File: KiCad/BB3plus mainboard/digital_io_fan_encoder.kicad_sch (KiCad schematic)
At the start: 51 parts, among them IC10 THVD1420DR, IC11 TPD4E001DRLR, IC12 TPD4E001DRLR, IC7 EMC2301-1-ACZL-TR, IC8 ISO6763FDWR, IC9 BD00FC0W, SW2 PEC16-2215F-S0024, X13 22-27-2031, X14 TBP03R1-350-10BE

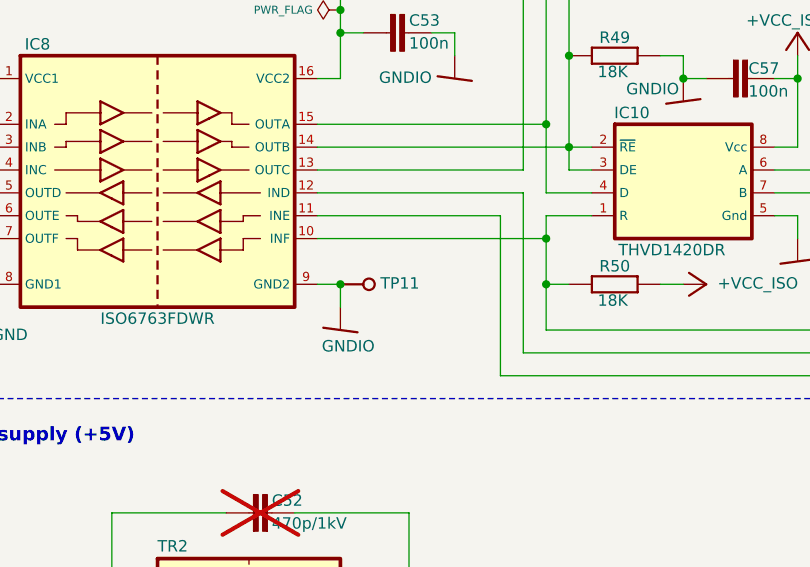
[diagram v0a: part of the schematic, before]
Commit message: Rear USB & Ethernet updated
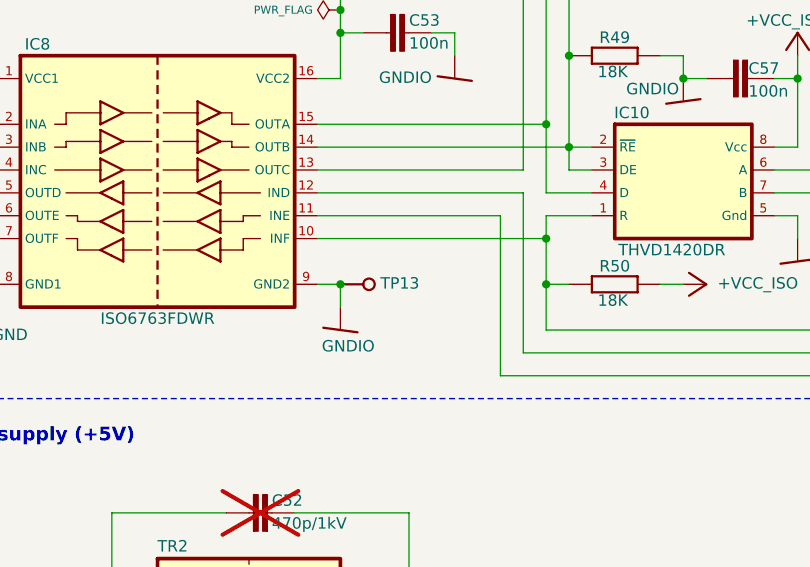
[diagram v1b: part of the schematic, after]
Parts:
- renumbered TP11 to TP13
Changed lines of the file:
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@@
 		(in_bom no)
 		(on_board yes)
-		(in_pos_files yes)
+		(in_pos_files no)
 		(dnp no)
-		(property "Reference" "TP11"
+		(property "Reference" "TP13"
 			(at 90.805 71.755 0)
 			(show_name no)
@@
 			(project "BB3plus mainboard"
 				(path "/1df84e4f-233a-4f72-9418-c0020706bb76/830c9101-e201-40d1-8c34-0dbed89b71c3"
-					(reference "TP11")
+					(reference "TP13")
 					(unit 1)
 				)

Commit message: BOM updated
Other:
- note added: "Alternative models: Aimtec M1SS-0503SLPZ, AM1SS-0503SEZ Gaptec 1S4E_0503S1U Traco power TBA 1-0510"
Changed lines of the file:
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@@
 	(title_block
 		(title "${project_name}")
-		(date "2026-10-16")
+		(date "2026-10-18")
 		(rev "${project_version}")
 		(company "${project_creator}")
@@
 		)
 	)
+	(text "Alternative models:\nAimtec M1SS-0503SLPZ, AM1SS-0503SEZ\nGaptec 1S4E_0503S1U\nTraco power TBA 1-0510\n"
+		(exclude_from_sim no)
+		(at 114.3 99.06 0)
+		(effects
+			(font
+				(size 0.889 0.889)
+				(color 132 0 132 1)
+			)
+			(justify left top)
+		)
+	)

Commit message: #28
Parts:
- removed JP10: (no value), PCM_EEZ_SMD:JP2 open (0603), symbol PCM_EEZ_unsorted:JP2 open

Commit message: Wire harness added, BOM updated
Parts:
- added KN1: A3123068, symbol PCM_EEZ_unsorted:A3123068
- added KN2: A3223007, symbol PCM_EEZ_unsorted:A3223007

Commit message: BOM update (knob), mechanical folder added
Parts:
- KN1: value A3123068 -> A3131068; Label (none) -> Knob; polyamide; Ø31x16mm; grey; TME A3123068 -> A3131068
- KN2: value A3223007 -> A3231007; Label (none) -> Cap; polyamide; grey; push-in; TME A3223007 -> A3231007
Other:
- moved on the sheet: KN2
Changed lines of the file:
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@@
 	(title_block
 		(title "${project_name}")
-		(date "2026-10-22")
+		(date "2026-10-25")
 		(rev "${project_version}")
 		(company "${project_creator}")
@@
 	(text_box "Encoder shaft length: 15 mm / Flatted"
 		(exclude_from_sim no)
-		(at 210.82 142.24 0)
+		(at 210.82 139.7 0)
 		(size 30.48 2.7636)
 		(margins 0.6667 0.6667 0.6667 0.6667)
@@
 		(in_pos_files no)
 		(dnp no)
-		(fields_autoplaced yes)
 		(property "Reference" "KN1"
-			(at 233.68 156.8449 0)
+			(at 233.045 156.21 0)
 			(show_name no)
 			(do_not_autoplace no)
@@
 			)
 		)
-		(property "Value" "A3123068"
-			(at 233.68 159.3849 0)
+		(property "Value" "A3131068"
+			(at 233.045 158.115 0)
 			(show_name no)
 			(do_not_autoplace no)
@@
 			)
 		)
-		(property "TME" "A3123068"
+		(property "TME" "A3131068"
 			(at 223.52 172.72 0)
 			(hide yes)
@@
 			)
 		)
+		(property "Label" "Knob; polyamide; Ø31x16mm; grey"
+			(at 233.045 160.655 0)
+			(show_name no)
+			(do_not_autoplace no)
+			(effects
+				(font
+					(size 0.889 0.889)
+				)
+				(justify left bottom)
+			)
+		)
 		(instances
 			(project "BB3plus mainboard"
@@
 	(symbol
 		(lib_id "PCM_EEZ_unsorted:A3223007")
-		(at 223.52 149.86 0)
+		(at 223.52 147.32 0)
 		(unit 1)
 		(body_style 1)
@@
 		(dnp no)
 		(property "Reference" "KN2"
-			(at 232.41 149.225 0)
+			(at 232.41 146.05 0)
 			(show_name no)
 			(do_not_autoplace no)
@@
 			)
 		)
-		(property "Value" "A3223007"
-			(at 232.41 151.765 0)
+		(property "Value" "A3231007"
+			(at 232.41 147.955 0)
 			(show_name no)
 			(do_not_autoplace no)
@@
 		)
 		(property "Footprint" ""
-			(at 223.52 149.86 0)
+			(at 223.52 147.32 0)
 			(hide yes)
 			(show_name no)
@@
 		)
 		(property "Datasheet" ""
-			(at 223.52 149.86 0)
+			(at 223.52 147.32 0)
 			(hide yes)
 			(show_name no)
@@
 		)
 		(property "Description" "Knob head cap; polyamide; grey"
-			(at 223.52 154.94 0)
+			(at 223.52 152.4 0)
 			(hide yes)
 			(show_name no)
@@
 		)
 		(property "DigiKey" "-"
-			(at 223.52 157.48 0)
+			(at 223.52 154.94 0)
 			(hide yes)
 			(show_name yes)
@@
 		)
 		(property "Mouser" "-"
-			(at 223.52 160.02 0)
+			(at 223.52 157.48 0)
 			(hide yes)
 			(show_name yes)
@@
 			)
 		)
-		(property "TME" "A3223007"
-			(at 223.52 162.56 0)
+		(property "TME" "A3231007"
+			(at 223.52 160.02 0)
 			(hide yes)
 			(show_name yes)
@@
 		)
 		(property "LCSC" "-"
-			(at 223.52 165.1 0)
+			(at 223.52 162.56 0)
 			(hide yes)
 			(show_name yes)
@@
 			)
 		)
+		(property "Label" "Cap; polyamide; grey; push-in"
+			(at 232.41 150.495 0)
+			(show_name no)
+			(do_not_autoplace no)
+			(effects
+				(font
+					(size 0.889 0.889)
+				)
+				(justify left bottom)
+			)
+		)

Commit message: BOM and DIB2 specification updated
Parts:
- C46, C48, C54: DigiKey 490-5523-1-ND -> 490-GRM21BR61E106MA73KCT-ND; Mouser 81-GRM21BR61E106KA3L -> 81-GRM21BR61C106KE5K; TME GRM21BR61E106KA73L -> CL21A106KAYNNNE
- C47, C49, C53, C57, C63: DigiKey 490-4774-1-ND -> 1276-6717-1-ND
- C51, C56, C58: DigiKey 1276-1860-1-ND -> 1276-1859-1-ND; TME CL10A105KB8NNNC -> CL10A105KB8NNNC
- C59: DigiKey 1276-1018-2-ND -> 1276-1018-1-ND; LCSC (none) -> C1588; TME CL10B102KB8NNNC -> C0805C102J5GAC
- C60, C61: DigiKey 311-3627-2-ND -> 311-3627-1-ND; Mouser 603-CC126JKNPOCBN330 -> 791-1206N330J102CT
- IC10: TME THVD1420DR -> -
- IC9: DigiKey BD00FC0WFP-E2TR-ND -> BD00FC0WFP-E2CT-ND
- L7: DigiKey 490-5137-2-ND -> 490-5137-1-ND
- R44: renamed from R43; DigiKey 13-RC0603FR-134K7LTR-ND -> 311-4.70KHRCT-ND
- R45: renamed from R44; DigiKey 13-RC0603FR-134K7LTR-ND -> 311-4.70KHRCT-ND
- R47: renamed from R46; DigiKey RC0603FR-073K3P -> YAG1300CT-ND
- R48: renamed from R47; DigiKey RC0603FR-073K3P -> YAG1300CT-ND
- R53: renamed from R52; Mouser 603-RC0603FR-10100RL -> 603-RC0603FR-100RL; TME RC0603FR-10100RL -> CRCW0603100RFKTABC
- R54: renamed from R53; DigiKey 1712-CRGH0603F10KCT-ND -> 13-RC0603FR-1310KLCT-ND; Mouser 756-WCR0603-10KFI -> 603-RC0603FR-1310KL; TME SMD0603-10K-1% -> RC0603FR-0710K
- R55: renamed from R54; DigiKey 1712-CRGH0603F10KCT-ND -> 13-RC0603FR-1310KLCT-ND; Mouser 756-WCR0603-10KFI -> 603-RC0603FR-1310KL; TME SMD0603-10K-1% -> RC0603FR-0710K
- R56: renamed from R55; DigiKey 1712-CRGH0603F10KCT-ND -> 13-RC0603FR-1310KLCT-ND; Mouser 756-WCR0603-10KFI -> 603-RC0603FR-1310KL; TME SMD0603-10K-1% -> RC0603FR-0710K
- R57: renamed from R56; DigiKey 1712-CRGH0603F10KCT-ND -> 13-RC0603FR-1310KLCT-ND; Mouser 756-WCR0603-10KFI -> 603-RC0603FR-1310KL; TME SMD0603-10K-1% -> RC0603FR-0710K
- renumbered KN2 to KN1, KN1 to KN2, R45 to R46, R48 to R49, R49 to R50, R50 to R51, R51 to R52
